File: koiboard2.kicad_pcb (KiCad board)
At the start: 2 copper layers, 227 x 75.4 mm, 140 parts, among them J1 Conn_01x04, J2 USB_C_Receptacle_USB2.0_16P, J3 Conn_01x05, SW1 choc_v1_SW_HS, SW10 choc_v1_SW_HS, SW11 choc_v1_SW_HS, SW12 choc_v1_SW_HS, SW13 choc_v1_SW_HS, SW14 choc_v1_SW_HS, SW15 choc_v1_SW_HS, SW16 choc_v1_SW_HS, SW17 choc_v1_SW_HS, SW18 choc_v1_SW_HS, SW19 choc_v1_SW_HS, SW2 choc_v1_SW_HS, SW20 choc_v1_SW_HS, SW21 choc_v1_SW_HS, SW22 choc_v1_SW_HS, SW23 choc_v1_SW_HS, SW24 choc_v1_SW_HS, SW25 choc_v1_SW_HS, SW26 choc_v1_SW_HS, SW27 choc_v1_SW_HS, SW28 choc_v1_SW_HS, SW29 choc_v1_SW_HS, SW3 choc_v1_SW_HS, SW30 choc_v1_SW_HS, SW31 choc_v1_SW_HS, SW32 choc_v1_SW_HS, SW33 choc_v1_SW_HS, SW34 choc_v1_SW_HS, SW35 choc_v1_SW_HS, SW36 choc_v1_SW_HS, SW37 choc_v1_SW_HS, SW38 choc_v1_SW_HS, SW39 choc_v1_SW_HS, SW4 choc_v1_SW_HS, SW40 choc_v1_SW_HS, SW41 choc_v1_SW_HS, SW42 choc_v1_SW_HS, SW43 choc_v1_SW_HS, SW44 choc_v1_SW_HS, SW45 choc_v1_SW_HS, SW46 choc_v1_SW_HS, SW47 choc_v1_SW_HS, SW48 choc_v1_SW_HS, SW49 choc_v1_SW_HS, SW5 choc_v1_SW_HS, SW6 choc_v1_SW_HS, SW7 choc_v1_SW_HS, SW8 choc_v1_SW_HS, SW9 choc_v1_SW_HS, U1 XC6206PxxxMR, U2 SRV05-4, U3 RP2040, U4 W25Q128JVS, Y1 Crystal_GND24

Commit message: update from review
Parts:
- BOOT1, RST1: footprint Button_Switch_SMD:SW_SPST_TL3342 -> Library:SW_SPST_TL3342
- C1, C10, C12, C13, C14, C2, C5, C6, C7, C8, C9: footprint Capacitor_SMD:C_0402_1005Metric -> Library:C_0402_1005Metric
- C11, C4: value 1u -> 100n; footprint Capacitor_SMD:C_0402_1005Metric -> Library:C_0402_1005Metric
- C15, C16: value 22p -> 33p; footprint Capacitor_SMD:C_0402_1005Metric -> Library:C_0402_1005Metric
- C3: footprint Capacitor_SMD:C_0603_1608Metric -> Library:C_0603_1608Metric
- D1, D10, D11, D12, D13, D14, D15, D16, D17, D18, D19, D2, D20, D21, D22, D23, D24, D25, D26, D27, D28, D29, D3, D30, D31, D32, D33, D34, D35, D36, D37, D38, D39, D4, D40, D41, D42, D43, D44, D45, D46, D47, D48, D49, D5, D6, D7, D8, D9: footprint Diode_SMD:D_SOD-123 -> Library:D_SOD-123
- F1: footprint Fuse:Fuse_1206_3216Metric -> Library:Fuse_1206_3216Metric
- H1, H2, H3, H4, H5, H6: footprint MountingHole:MountingHole_3.2mm_M3_ISO14580 -> Library:MountingHole_3.2mm_M3_ISO14580
- J1: footprint Connector_JST:JST_SH_SM04B-SRSS-TB_1x04-1MP_P1.00mm_Horizontal -> Library:JST_SH_SM04B-SRSS-TB_1x04-1MP_P1.00mm_Horizontal
- J2: footprint Connector_USB:USB_C_Receptacle_HRO_TYPE-C-31-M-12 -> Library:USB_C_Receptacle_HRO_TYPE-C-31-M-12
- J3: footprint Cool Library:PinHeader_1x05_P2.54mm_Vertical_No_3D_Header -> Library:PinHeader_1x05_P2.54mm_Vertical_No_3D_Header
- R1, R2, R3, R4, R5, R6, R7, R8, R9: footprint Resistor_SMD:R_0402_1005Metric -> Library:R_0402_1005Metric
- SW1, SW10, SW11, SW12, SW13, SW14, SW15, SW16, SW17, SW18, SW19, SW2, SW20, SW21, SW22, SW23, SW24, SW25, SW26, SW27, SW28, SW29, SW3, SW30, SW31, SW32, SW33, SW34, SW35, SW36, SW37, SW38, SW39, SW4, SW40, SW41, SW43, SW45, SW46, SW47, SW48, SW49, SW5, SW6, SW7, SW8, SW9: footprint PCM_marbastlib-xp-choc:SW_choc_v2_HS_CPG135001S30_1u -> Library:SW_choc_v2_HS_CPG135001S30_1u
- SW42, SW44: footprint Cool Library:SW_choc_v2_HS_CPG135001S30_1u_switch_hide -> Library:SW_choc_v2_HS_CPG135001S30_1u_switch_hide
- U1: footprint Package_TO_SOT_SMD:SOT-23-3 -> Library:SOT-23-3
- U2: footprint PCM_marbastlib-various:SOT-23-6-routable -> Library:SOT-23-6-routable
- U3: footprint Package_DFN_QFN:QFN-56-1EP_7x7mm_P0.4mm_EP3.2x3.2mm -> Library:QFN-56-1EP_7x7mm_P0.4mm_EP3.2x3.2mm
- U4: footprint Package_SO:SOIC-8_5.3x5.3mm_P1.27mm -> Library:SOIC-8_5.3x5.3mm_P1.27mm
- Y1: footprint Crystal:Crystal_SMD_3225-4Pin_3.2x2.5mm -> Library:Crystal_SMD_3225-4Pin_3.2x2.5mm
- moved C3 1.74 mm to (133.3, 55.4)
- moved C12 0.97 mm to (111.1, 63.5)
- turned R3 to 0 degrees
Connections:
- R3 pad 1: Net-(R3-Pad1) -> +3V3
- R3 pad 2: +3V3 -> Net-(R3-Pad2)
- R5 pad 2: Net-(R3-Pad1) -> Net-(R3-Pad2)
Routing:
- net GND: track 80.1 -> 98.0 mm, vias 105 -> 104
- net Q_IO0: track 18.7 -> 24.5 mm
- net Net-(BOOT1-Pad2): track 9.46 -> 15.1 mm
- net +5V: track 51.2 -> 54.1 mm
- net Q_SEL: track 59.0 -> 61.5 mm
- net Q_IO1: track 22.9 -> 25.3 mm
- net Q_IO2: track 22.5 -> 24.9 mm
- net Q_CLK: track 20.7 -> 22.9 mm
- net Net-(R3-Pad2): track 0.00 -> 1.19 mm
- net Net-(R3-Pad1): track 1.19 -> 0.00 mm
- net Q_IO3: track 23.2 -> 24.0 mm
- net COL6: track 85.5 -> 84.9 mm

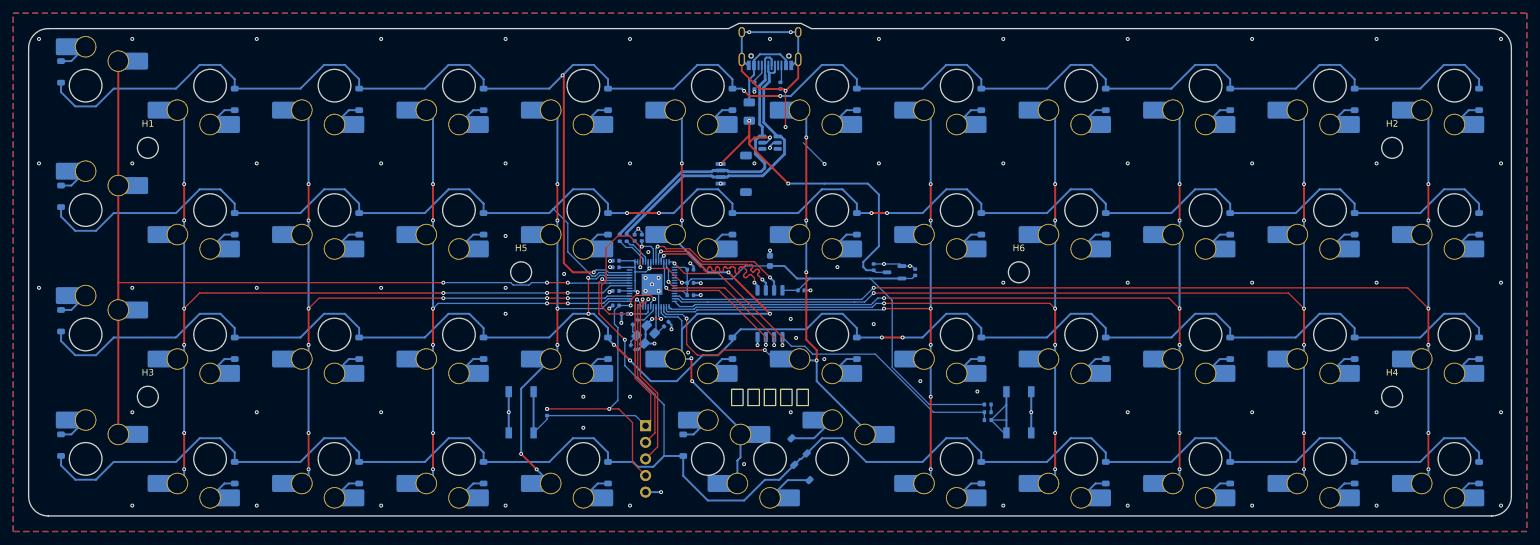
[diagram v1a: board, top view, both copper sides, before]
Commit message: 4 layers
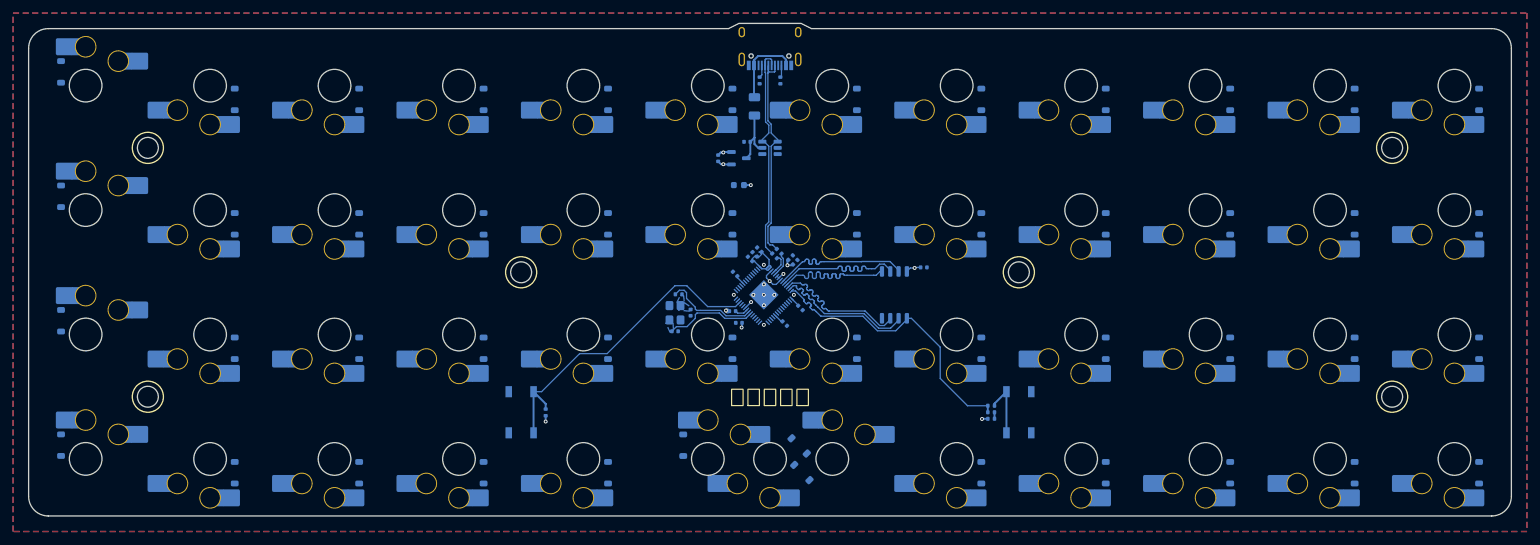
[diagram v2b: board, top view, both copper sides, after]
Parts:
- removed J2: USB_C_Receptacle_USB2.0_16P, Library:USB_C_Receptacle_HRO_TYPE-C-31-M-12
- removed J3: Conn_01x05, Library:PinHeader_1x05_P2.54mm_Vertical_No_3D_Header
- J1: value Conn_01x04 -> USB_C_Receptacle_USB2.0_16P; footprint Library:JST_SH_SM04B-SRSS-TB_1x04-1MP_P1.00mm_Horizontal -> Library:USB_C_Receptacle_HRO_TYPE-C-31-M-12
- moved C2 34.9 mm to (125.4, 39.7), turned to -90 degrees
- moved U1 29.5 mm to (128.6, 39.7), turned to 0 degrees
- moved C9 27.6 mm to (135.6, 65.0), turned to -45 degrees
- moved C1 27.3 mm to (129.8, 37.2), turned to 180 degrees
- moved C12 26.8 mm to (136.5, 54.9), turned to 45 degrees
- moved R7 23.9 mm to (134.0, 54.6), turned to -45 degrees
- moved C13 23.8 mm to (137.2, 55.6), turned to 45 degrees
- moved R8 23.4 mm to (134.7, 53.9), turned to -45 degrees
- moved C4 22.1 mm to (131.7, 53.7), turned to 135 degrees
- moved J1 21.4 mm to (133.3, 21.4), turned to 0 degrees
- moved C6 21.1 mm to (130.3, 55.1), turned to 135 degrees
- moved C11 20.6 mm to (128.6, 64.9), turned to 180 degrees
- moved U4 19.3 mm to (152.4, 60.6)
- moved C14 19.1 mm to (156.9, 56.4)
- moved C8 17.9 mm to (127.6, 63.1)
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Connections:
- net Net-(C16-Pad2) renamed /Crystal/Y1 - R9
- R1 pad 1: Net-(J2-CC1) -> Net-(J1-CC1)
- R2 pad 1: Net-(J2-CC2) -> Net-(J1-CC2)
- R7 pad 2: Net-(U3-USB_DM) -> D-
- R8 pad 2: Net-(U3-USB_DP) -> D+
- U3 pad 12: COL11 -> unconnected-(U3-GPIO9-Pad12)
- U3 pad 13: COL10 -> unconnected-(U3-GPIO10-Pad13)
- U3 pad 14: COL9 -> unconnected-(U3-GPIO11-Pad14)
- U3 pad 15: COL8 -> unconnected-(U3-GPIO12-Pad15)
- U3 pad 16: COL7 -> unconnected-(U3-GPIO13-Pad16)
- U3 pad 17: COL6 -> unconnected-(U3-GPIO14-Pad17)
- U3 pad 18: COL5 -> unconnected-(U3-GPIO15-Pad18)
- U3 pad 29: COL4 -> unconnected-(U3-GPIO18-Pad29)
- U3 pad 30: COL3 -> unconnected-(U3-GPIO19-Pad30)
- U3 pad 31: COL2 -> unconnected-(U3-GPIO20-Pad31)
- U3 pad 35: COL1 -> unconnected-(U3-GPIO23-Pad35)
- U3 pad 36: COL0 -> unconnected-(U3-GPIO24-Pad36)
- U3 pad 37: ROW3 -> unconnected-(U3-GPIO25-Pad37)
- U3 pad 38: ROW2 -> unconnected-(U3-GPIO26/ADC0-Pad38)
- U3 pad 39: ROW1 -> unconnected-(U3-GPIO27/ADC1-Pad39)
- U3 pad 40: ROW0 -> unconnected-(U3-GPIO28/ADC2-Pad40)
- U3 pad 46: Net-(U3-USB_DM) -> D-
- U3 pad 47: Net-(U3-USB_DP) -> D+
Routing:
- net ROW0: track 303.7 -> 0.00 mm, vias 4 -> 0
- net ROW3: track 302.0 -> 0.00 mm, vias 2 -> 0
- net ROW1: track 281.8 -> 0.00 mm, vias 4 -> 0
- net ROW2: track 277.6 -> 0.00 mm, vias 6 -> 0
- net COL11: track 177.3 -> 0.00 mm, vias 7 -> 0
- net COL10: track 157.8 -> 0.00 mm, vias 7 -> 0
- net COL9: track 138.5 -> 0.00 mm, vias 7 -> 0
- net COL0: track 135.7 -> 0.00 mm, vias 3 -> 0
- net +3V3: track 154.2 -> 21.3 mm, vias 7 -> 6
- net COL1: track 129.4 -> 0.00 mm, vias 9 -> 0
- net COL8: track 119.6 -> 0.00 mm, vias 7 -> 0
- net COL2: track 109.6 -> 0.00 mm, vias 9 -> 0
- net COL7: track 101.0 -> 0.00 mm, vias 7 -> 0
- net GND: track 98.0 -> 2.23 mm, vias 104 -> 11
- net COL3: track 90.4 -> 0.00 mm, vias 8 -> 0
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- added copper zone on In1.Cu, net +1V1
- added copper zone on B.Cu, net +3V3
- added copper zone on In1.Cu, net +3V3
- added copper zone on B.Cu, net /Crystal/Y1 - R9
- added copper zone on In2.Cu, net GND
- added copper zone on B.Cu, net XIN
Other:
- copper layers 2 -> 4

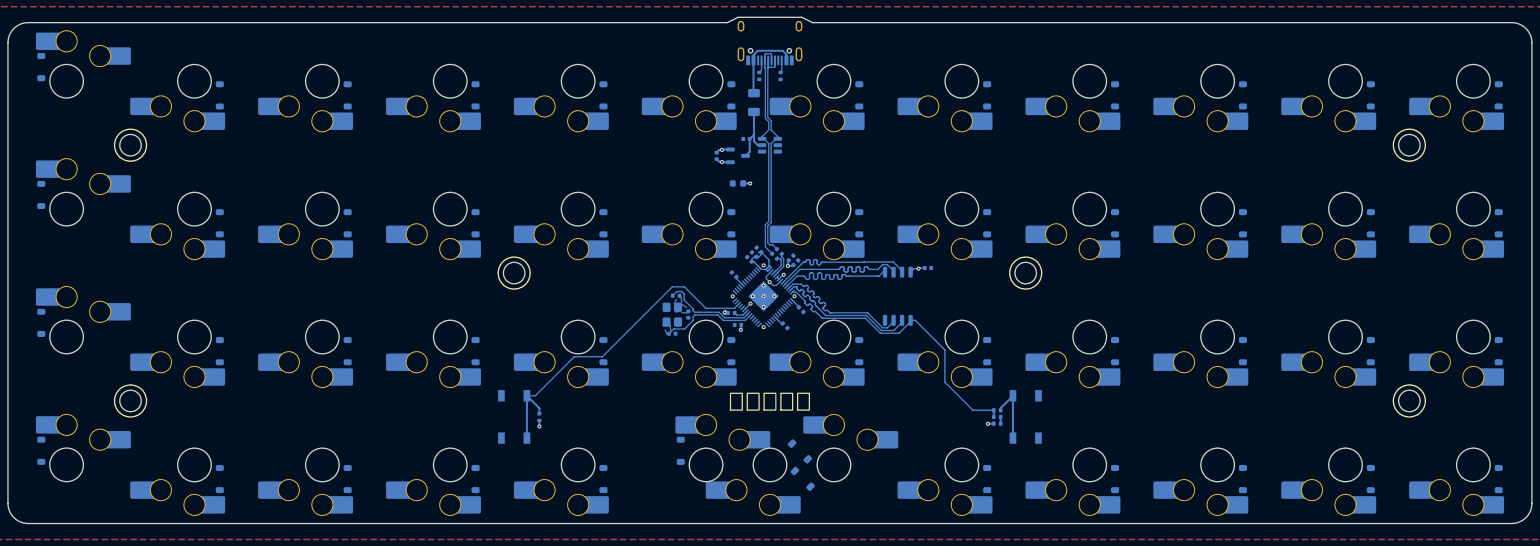
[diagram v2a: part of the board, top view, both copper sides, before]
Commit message: routed matrix
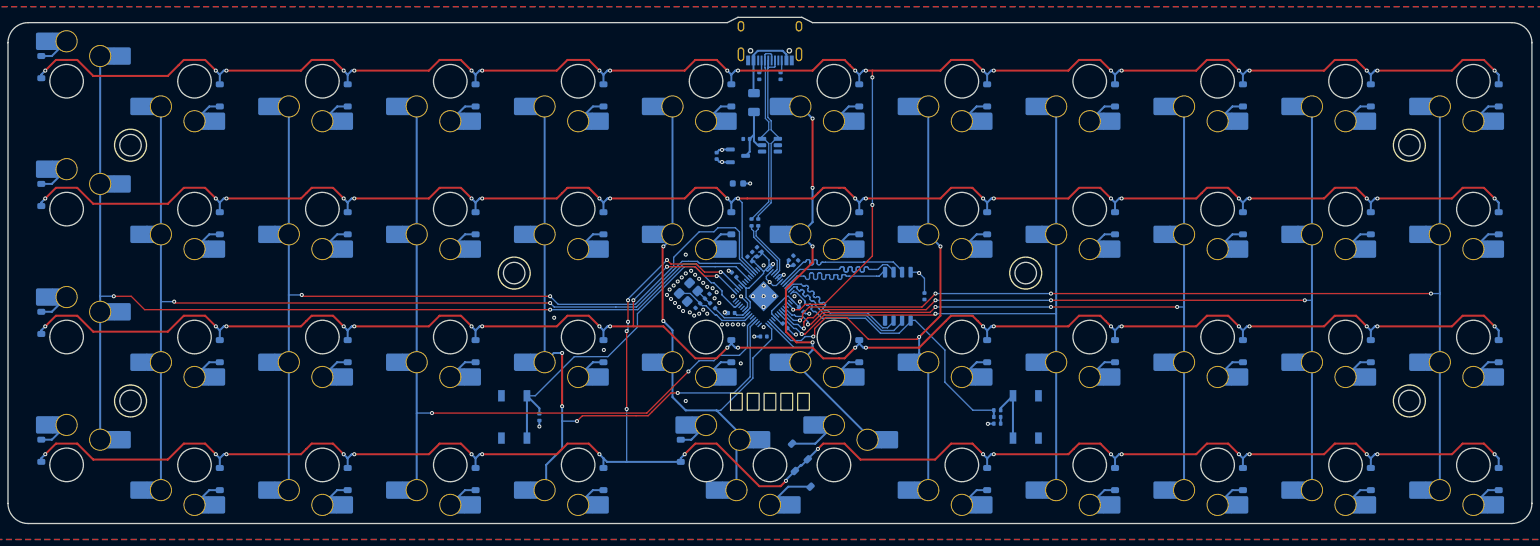
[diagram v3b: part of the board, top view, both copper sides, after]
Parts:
- moved R7 6.10 mm to (130.6, 49.6), turned to -90 degrees
- moved C15 5.65 mm to (122.6, 62.0), turned to 45 degrees
- moved R9 5.63 mm to (124.8, 62.0), turned to -45 degrees
- moved R8 5.36 mm to (131.6, 49.6), turned to -90 degrees
- moved C14 4.23 mm to (156.4, 60.6), turned to -90 degrees
- moved C11 4.19 mm to (132.4, 66.6), turned to 0 degrees
- moved Y1 4.12 mm to (121.2, 60.0), turned to -135 degrees
- moved C16 3.92 mm to (124.0, 60.6), turned to -135 degrees
- moved C6 0.07 mm to (130.3, 55.0)
- moved C4 0.07 mm to (131.8, 53.6)
- moved C5 0.07 mm to (131.0, 54.3)
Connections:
- R7 pad 2: D- -> Net-(U3-USB_DM)
- R8 pad 2: D+ -> Net-(U3-USB_DP)
- U3 pad 12: unconnected-(U3-GPIO9-Pad12) -> COL7
- U3 pad 13: unconnected-(U3-GPIO10-Pad13) -> COL6
- U3 pad 14: unconnected-(U3-GPIO11-Pad14) -> COL5
- U3 pad 17: unconnected-(U3-GPIO14-Pad17) -> COL4
- U3 pad 18: unconnected-(U3-GPIO15-Pad18) -> COL3
- U3 pad 24: SWC -> unconnected-(U3-SWCLK-Pad24)
- U3 pad 25: SWD -> unconnected-(U3-SWDIO-Pad25)
- U3 pad 29: unconnected-(U3-GPIO18-Pad29) -> ROW2
- U3 pad 3: unconnected-(U3-GPIO1-Pad3) -> ROW0
- U3 pad 31: unconnected-(U3-GPIO20-Pad31) -> ROW3
- U3 pad 36: unconnected-(U3-GPIO24-Pad36) -> COL0
- U3 pad 38: unconnected-(U3-GPIO26/ADC0-Pad38) -> COL1
- U3 pad 39: unconnected-(U3-GPIO27/ADC1-Pad39) -> COL2
- U3 pad 40: unconnected-(U3-GPIO28/ADC2-Pad40) -> ROW1
- U3 pad 46: D- -> Net-(U3-USB_DM)
- U3 pad 47: D+ -> Net-(U3-USB_DP)
- U3 pad 5: unconnected-(U3-GPIO3-Pad5) -> COL9
- U3 pad 6: unconnected-(U3-GPIO4-Pad6) -> COL11
- U3 pad 7: unconnected-(U3-GPIO5-Pad7) -> COL10
- U3 pad 8: unconnected-(U3-GPIO6-Pad8) -> COL8
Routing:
- net ROW3: track 0.00 -> 302.0 mm, vias 0 -> 26
- net ROW0: track 0.00 -> 299.3 mm, vias 0 -> 25
- net ROW2: track 0.00 -> 278.9 mm, vias 0 -> 25
- net ROW1: track 0.00 -> 267.4 mm, vias 0 -> 22
- net COL0: track 0.00 -> 158.3 mm, vias 0 -> 2
- net COL11: track 0.00 -> 157.7 mm, vias 0 -> 4
- net COL1: track 0.00 -> 149.2 mm, vias 0 -> 2
- net COL10: track 0.00 -> 139.6 mm, vias 0 -> 4
- net COL2: track 0.00 -> 137.7 mm, vias 0 -> 2
- net COL9: track 0.00 -> 119.0 mm, vias 0 -> 4
- net COL3: track 0.00 -> 115.1 mm, vias 0 -> 2
- net COL4: track 0.00 -> 102.2 mm, vias 0 -> 4
- net COL8: track 0.00 -> 101.0 mm, vias 0 -> 2
- net COL7: track 0.00 -> 86.5 mm, vias 0 -> 3
- net COL5: track 0.00 -> 82.1 mm, vias 0 -> 2
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- removed copper zone on B.Cu, net /Crystal/Y1 - R9
- removed copper zone on B.Cu, net XIN

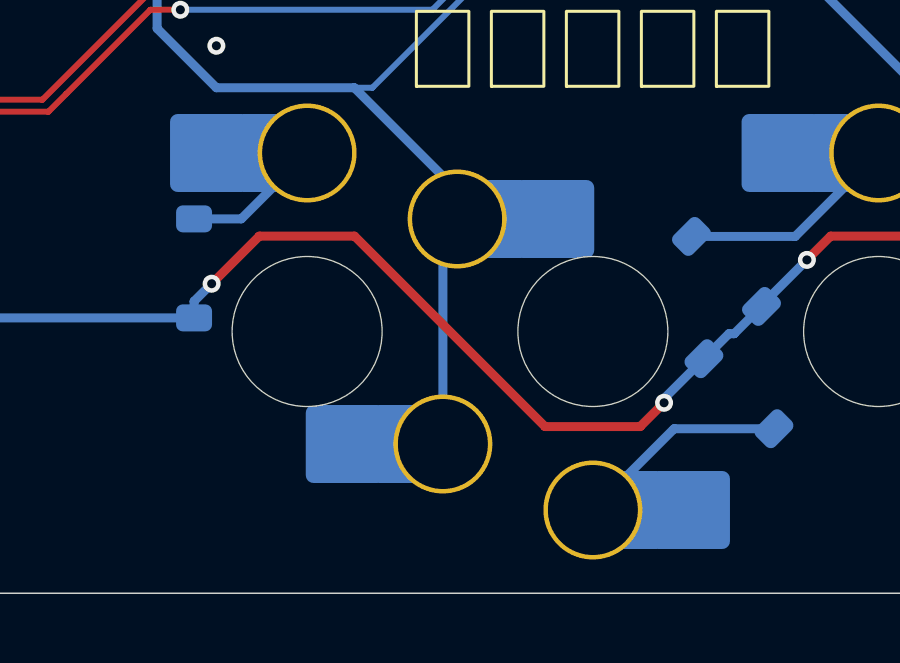
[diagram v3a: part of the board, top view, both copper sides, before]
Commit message: drc errors fix
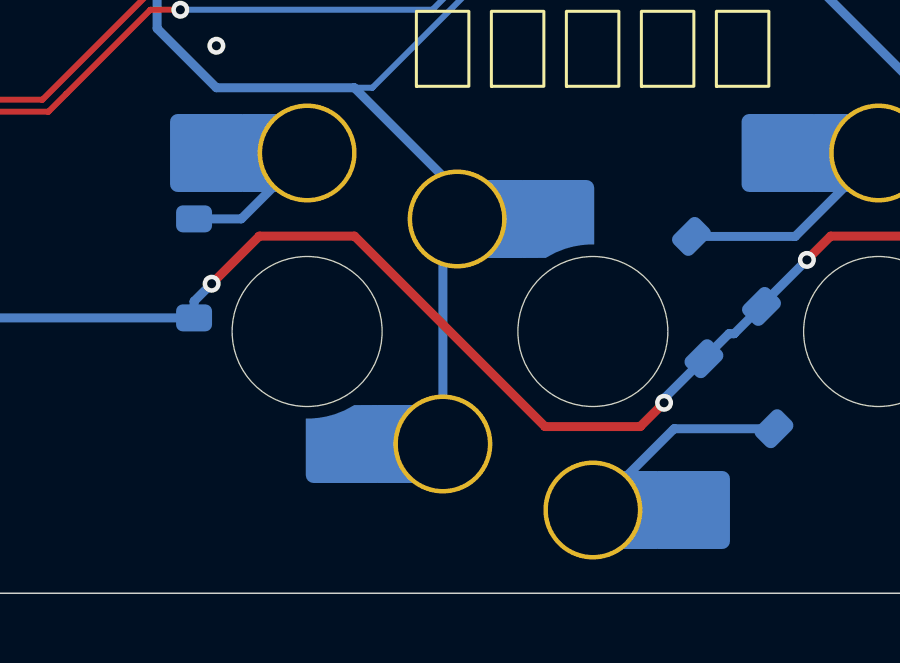
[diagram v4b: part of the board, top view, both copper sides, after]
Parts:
- SW42: footprint Library:SW_choc_v2_HS_CPG135001S30_1u_switch_hide -> Library:SW_choc_v2_HS_CPG135001S30_1u_SW42
- SW43: footprint Library:SW_choc_v2_HS_CPG135001S30_1u -> Library:SW_choc_v2_HS_CPG135001S30_1u_SW42_switch_show
